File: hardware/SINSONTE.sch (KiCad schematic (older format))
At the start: 31 parts, among them J1 BAT, J10 Conn_01x01_Male, J11 Conn_01x01_Male, J12 Conn_01x04_Male, J13 Conn_01x01_Male, J14 Conn_01x02_Male, J2 CLOCK, J3 LIGHT_SENSOR, J4 Conn_01x17_Male, J5 Conn_01x01_Male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

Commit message: add note to change R1 for CP
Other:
- note added: "Increase to 470K\nfor CircuitPython"
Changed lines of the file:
@@
 Wire Wire Line
 	6950 5000 9000 5000
+Text Notes 3150 3350 0    50   ~ 0
+Increase to 470K\nfor CircuitPython
 $EndSCHEMATC

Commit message: changed ext batt for screw terminal type
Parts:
- J1: footprint Connector_PinHeader_2.54mm:PinHeader_1x02_P2.54mm_Vertical -> TerminalBlock_4Ucon:TerminalBlock_4Ucon_1x02_P3.50mm_Horizontal
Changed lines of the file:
@@
 F 0 "J1" H 2800 2800 50  0000 C CNN
 F 1 "BAT" H 2800 2700 50  0000 C CNN
-F 2 "Connector_PinHeader_2.54mm:PinHeader_1x02_P2.54mm_Vertical" H 2950 2750 50  0001 C CNN
+F 2 "TerminalBlock_4Ucon:TerminalBlock_4Ucon_1x02_P3.50mm_Horizontal" H 2950 2750 50  0001 C CNN
 F 3 "~" H 2950 2750 50  0001 C CNN
 	1    2950 2750

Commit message: rpi first half conn aded 1 pos on ground
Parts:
- removed J4: Conn_01x17_Male, Connector_PinHeader_2.54mm:PinHeader_1x17_P2.54mm_Vertical, symbol Connector:Conn_01x17_Male
- added J15: Conn_01x01_Male, Connector_PinHeader_2.54mm:PinHeader_1x01_P2.54mm_Vertical, symbol Connector:Conn_01x01_Male
- added J4: Conn_01x18_Male, Connector_PinHeader_2.54mm:PinHeader_1x18_P2.54mm_Vertical, symbol Connector:Conn_01x18_Male
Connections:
- wire segments 144 -> 146
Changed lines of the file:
@@
 	9000 3350 9000 5000
-$Comp
-L Connector:Conn_01x17_Male J4
-U 1 1 604C5DB6
-P 4550 3350
-F 0 "J4" H 4658 4331 50  0000 C CNN
-F 1 "Conn_01x17_Male" H 4658 4240 50  0000 C CNN
-F 2 "Connector_PinHeader_2.54mm:PinHeader_1x17_P2.54mm_Vertical" H 4550 3350 50  0001 C CNN
-F 3 "~" H 4550 3350 50  0001 C CNN
-	1    4550 3350
-	1    0    0    -1
-$EndComp
-Wire Wire Line
-	4750 2550 4900 2550
-Wire Wire Line
-	4750 2650 4900 2650
-Wire Wire Line
-	4750 2750 4800 2750
-Wire Wire Line
-	4750 2850 4900 2850
-Wire Wire Line
-	4750 2950 4900 2950
-Wire Wire Line
-	4750 3050 4900 3050
-Wire Wire Line
-	4750 3150 4900 3150
-Wire Wire Line
-	4750 3250 4800 3250
-Wire Wire Line
-	4750 3350 4900 3350
-Wire Wire Line
-	4750 3450 4900 3450
-Wire Wire Line
-	4750 3550 4900 3550
-Wire Wire Line
-	4750 3650 4900 3650
-Wire Wire Line
-	4750 3750 4800 3750
-Wire Wire Line
-	4750 3850 4900 3850
-Wire Wire Line
-	4750 3950 4900 3950
-Wire Wire Line
-	4750 4050 4900 4050
-Wire Wire Line
-	4750 4150 4900 4150
 $Comp
 L Connector:Conn_01x01_Male J5
@@
 Connection ~ 4800 4250
 Wire Wire Line
-	4800 4250 4600 4250
+	4800 4250 4700 4250
 Wire Wire Line
 	6400 3250 6450 3250
@@
 Text Notes 3150 3350 0    50   ~ 0
 Increase to 470K\nfor CircuitPython
+$Comp
+L Connector:Conn_01x18_Male J4
+U 1 1 618ACA73
+P 4500 3350
+F 0 "J4" H 4608 4331 50  0000 C CNN
+F 1 "Conn_01x18_Male" H 4608 4240 50  0000 C CNN
+F 2 "Connector_PinHeader_2.54mm:PinHeader_1x18_P2.54mm_Vertical" H 4500 3350 50  0001 C CNN
+F 3 "~" H 4500 3350 50  0001 C CNN
+	1    4500 3350
+	1    0    0    -1
+$EndComp
+Connection ~ 4700 4250
+Wire Wire Line
+	4700 4250 4600 4250
+Wire Wire Line
+	4700 2550 4900 2550
+Wire Wire Line
+	4700 2650 4900 2650
+Wire Wire Line
+	4700 2750 4800 2750
+Wire Wire Line
+	4700 2850 4900 2850
+Wire Wire Line
+	4700 2950 4900 2950
+Wire Wire Line
+	4700 3050 4900 3050
+Wire Wire Line
+	4700 3150 4900 3150
+Wire Wire Line
+	4700 3250 4800 3250
+Wire Wire Line
+	4700 3350 4900 3350
+Wire Wire Line
+	4700 3450 4900 3450
+Wire Wire Line
+	4700 3550 4900 3550
+Wire Wire Line
+	4700 3650 4900 3650
+Wire Wire Line
+	4700 3750 4800 3750
+Wire Wire Line
+	4700 3850 4900 3850
+Wire Wire Line
+	4700 3950 4900 3950
+Wire Wire Line
+	4700 4050 4900 4050
+Wire Wire Line
+	4700 4150 4900 4150
+$Comp
+L Connector:Conn_01x01_Male J15
+U 1 1 6193CA8B
+P 4500 4450
+F 0 "J15" H 4608 4631 50  0000 C CNN
+F 1 "Conn_01x01_Male" H 4608 4540 50  0000 C CNN
+F 2 "Connector_PinHeader_2.54mm:PinHeader_1x01_P2.54mm_Vertical" H 4500 4450 50  0001 C CNN
+F 3 "~" H 4500 4450 50  0001 C CNN
+	1    4500 4450
+	1    0    0    -1
+$EndComp
+Wire Wire Line
+	4700 4450 4800 4450
+Connection ~ 4800 4450
 $EndSCHEMATC

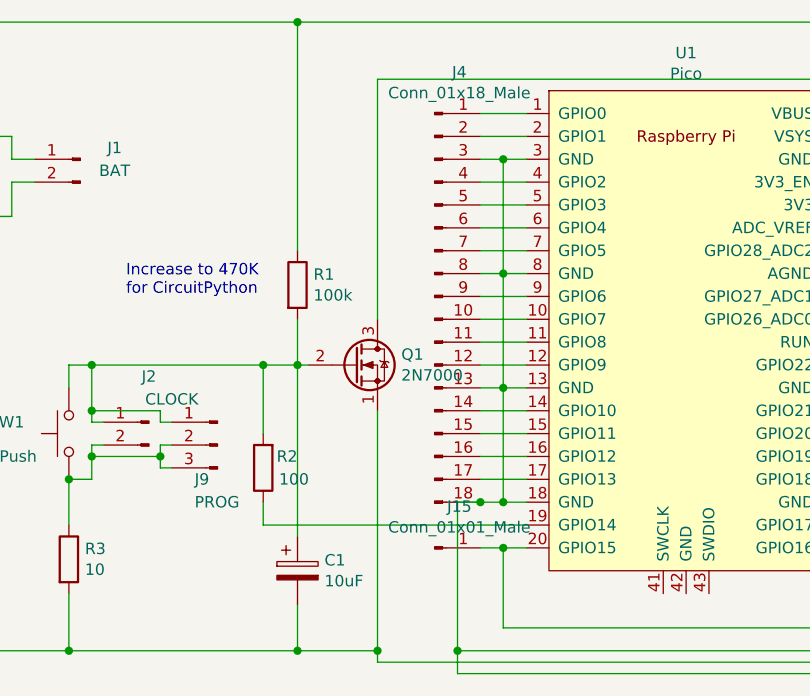
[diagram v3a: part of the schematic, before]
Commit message: rpi first half conn aded all pins connector
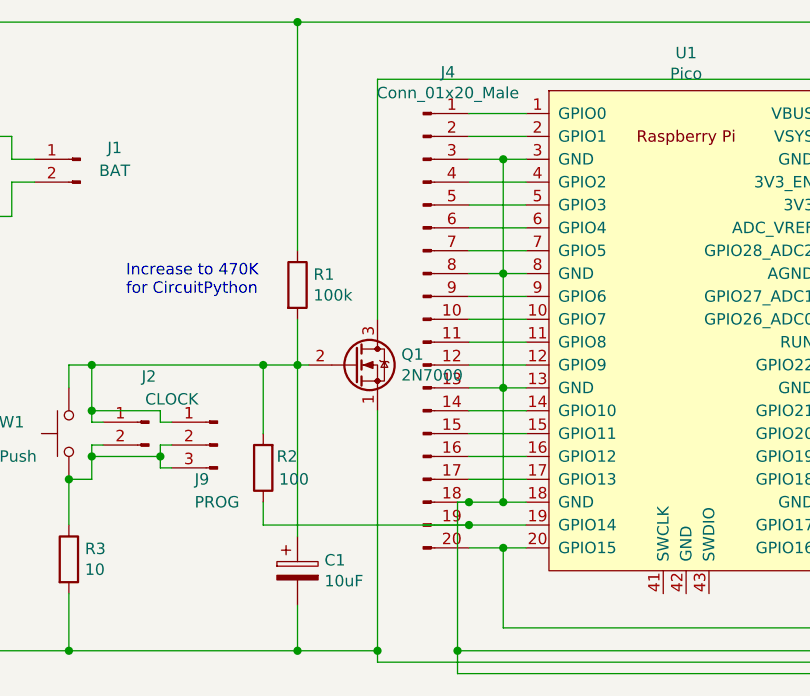
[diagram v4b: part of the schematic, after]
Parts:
- removed J15: Conn_01x01_Male, Connector_PinHeader_2.54mm:PinHeader_1x01_P2.54mm_Vertical, symbol Connector:Conn_01x01_Male
- removed J4: Conn_01x18_Male, Connector_PinHeader_2.54mm:PinHeader_1x18_P2.54mm_Vertical, symbol Connector:Conn_01x18_Male
- added J4: Conn_01x20_Male, Connector_PinHeader_2.54mm:PinHeader_1x20_P2.54mm_Vertical, symbol Connector:Conn_01x20_Male
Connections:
- net at U1.1 (GPIO0): now also J4.1 (Pin_1)
- net at U1.10 (GPIO7): now also J4.10 (Pin_10)
- net at U1.11 (GPIO8): now also J4.11 (Pin_11)
- net at U1.12 (GPIO9): now also J4.12 (Pin_12)
- net at BT1.2 (-), C1.2, C2.2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: now also J4.13 (Pin_13), J4.18 (Pin_18), J4.3 (Pin_3), J4.8 (Pin_8)
- net at U1.14 (GPIO10): now also J4.14 (Pin_14)
- net at U1.15 (GPIO11): now also J4.15 (Pin_15)
- net at U1.16 (GPIO12): now also J4.16 (Pin_16)
- net at U1.17 (GPIO13): now also J4.17 (Pin_17)
- net at R2.1, U1.19 (GPIO14): now also J4.19 (Pin_19)
- net at U1.2 (GPIO1): now also J4.2 (Pin_2)
- net at R8.1, U1.20 (GPIO15): now also J4.20 (Pin_20)
- net at U1.4 (GPIO2): now also J4.4 (Pin_4)
- net at U1.5 (GPIO3): now also J4.5 (Pin_5)
- net at U1.6 (GPIO4): now also J4.6 (Pin_6)
- net at U1.7 (GPIO5): now also J4.7 (Pin_7)
- net at U1.9 (GPIO6): now also J4.9 (Pin_9)
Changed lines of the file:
@@
 Connection ~ 3900 3650
 Wire Wire Line
-	3750 4350 4900 4350
+	3750 4350 4650 4350
 Wire Wire Line
 	3900 4700 3900 4900
@@
 Connection ~ 4800 4250
 Wire Wire Line
-	4800 4250 4700 4250
-Wire Wire Line
 	6400 3250 6450 3250
 Connection ~ 6400 3250
@@
 Text Notes 3150 3350 0    50   ~ 0
 Increase to 470K\nfor CircuitPython
-$Comp
-L Connector:Conn_01x18_Male J4
-U 1 1 618ACA73
-P 4500 3350
-F 0 "J4" H 4608 4331 50  0000 C CNN
-F 1 "Conn_01x18_Male" H 4608 4240 50  0000 C CNN
-F 2 "Connector_PinHeader_2.54mm:PinHeader_1x18_P2.54mm_Vertical" H 4500 3350 50  0001 C CNN
-F 3 "~" H 4500 3350 50  0001 C CNN
-	1    4500 3350
+Connection ~ 4800 4450
+Wire Wire Line
+	4600 4250 4650 4250
+$Comp
+L Connector:Conn_01x20_Male J4
+U 1 1 618AE8C2
+P 4450 3450
+F 0 "J4" H 4558 4531 50  0000 C CNN
+F 1 "Conn_01x20_Male" H 4558 4440 50  0000 C CNN
+F 2 "Connector_PinHeader_2.54mm:PinHeader_1x20_P2.54mm_Vertical" H 4450 3450 50  0001 C CNN
+F 3 "~" H 4450 3450 50  0001 C CNN
+	1    4450 3450
 	1    0    0    -1
 $EndComp
-Connection ~ 4700 4250
-Wire Wire Line
-	4700 4250 4600 4250
-Wire Wire Line
-	4700 2550 4900 2550
-Wire Wire Line
-	4700 2650 4900 2650
-Wire Wire Line
-	4700 2750 4800 2750
-Wire Wire Line
-	4700 2850 4900 2850
-Wire Wire Line
-	4700 2950 4900 2950
-Wire Wire Line
-	4700 3050 4900 3050
-Wire Wire Line
-	4700 3150 4900 3150
-Wire Wire Line
-	4700 3250 4800 3250
-Wire Wire Line
-	4700 3350 4900 3350
-Wire Wire Line
-	4700 3450 4900 3450
-Wire Wire Line
-	4700 3550 4900 3550
-Wire Wire Line
-	4700 3650 4900 3650
-Wire Wire Line
-	4700 3750 4800 3750
-Wire Wire Line
-	4700 3850 4900 3850
-Wire Wire Line
-	4700 3950 4900 3950
-Wire Wire Line
-	4700 4050 4900 4050
-Wire Wire Line
-	4700 4150 4900 4150
-$Comp
-L Connector:Conn_01x01_Male J15
-U 1 1 6193CA8B
-P 4500 4450
-F 0 "J15" H 4608 4631 50  0000 C CNN
-F 1 "Conn_01x01_Male" H 4608 4540 50  0000 C CNN
-F 2 "Connector_PinHeader_2.54mm:PinHeader_1x01_P2.54mm_Vertical" H 4500 4450 50  0001 C CNN
-F 3 "~" H 4500 4450 50  0001 C CNN
-	1    4500 4450
-	1    0    0    -1
-$EndComp
-Wire Wire Line
-	4700 4450 4800 4450
-Connection ~ 4800 4450
+Connection ~ 4650 4250
+Wire Wire Line
+	4650 4250 4800 4250
+Connection ~ 4650 4350
+Wire Wire Line
+	4650 4350 4900 4350
+Wire Wire Line
+	4650 2550 4900 2550
+Wire Wire Line
+	4650 2650 4900 2650
+Wire Wire Line
+	4650 2750 4800 2750
+Wire Wire Line
+	4650 2850 4900 2850
+Wire Wire Line
+	4650 2950 4900 2950
+Wire Wire Line
+	4650 3050 4900 3050
+Wire Wire Line
+	4650 3150 4900 3150
+Wire Wire Line
+	4650 3250 4800 3250
+Wire Wire Line
+	4650 3350 4900 3350
+Wire Wire Line
+	4650 3450 4900 3450
+Wire Wire Line
+	4650 3550 4900 3550
+Wire Wire Line
+	4650 3650 4900 3650
+Wire Wire Line
+	4650 3750 4800 3750
+Wire Wire Line
+	4650 3850 4900 3850
+Wire Wire Line
+	4650 3950 4900 3950
+Wire Wire Line
+	4650 4050 4900 4050
+Wire Wire Line
+	4650 4150 4900 4150
+Wire Wire Line
+	4650 4450 4800 4450
 $EndSCHEMATC

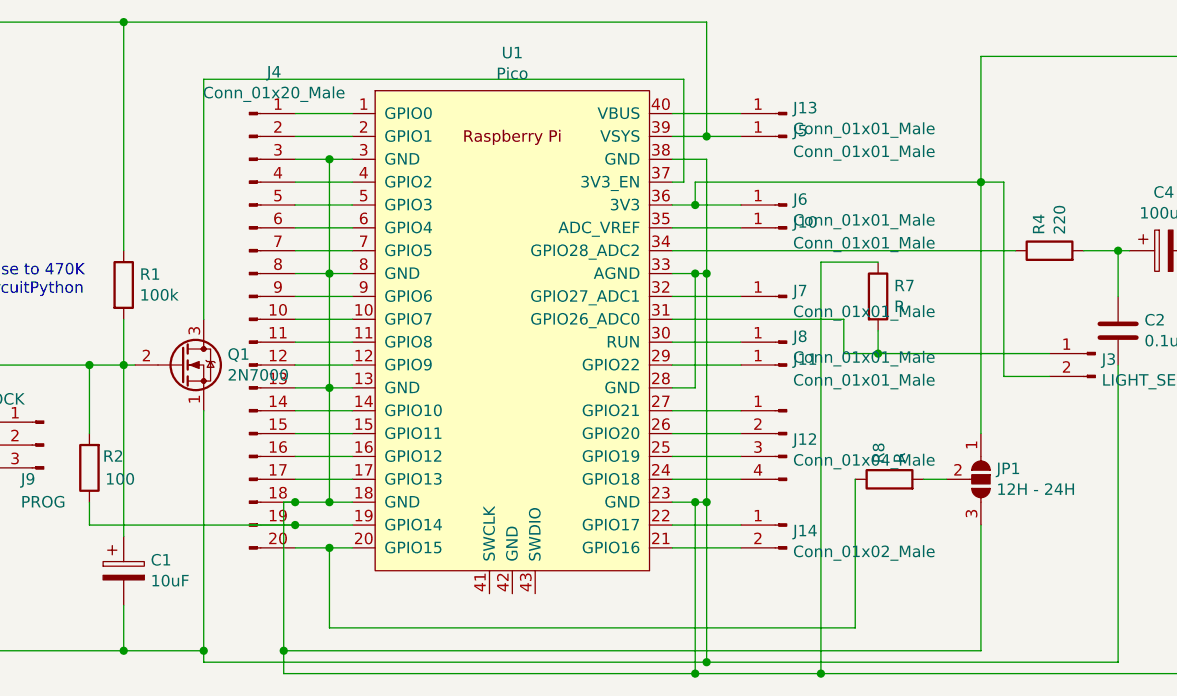
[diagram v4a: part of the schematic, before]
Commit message: rpi second half conn aded all pins connector
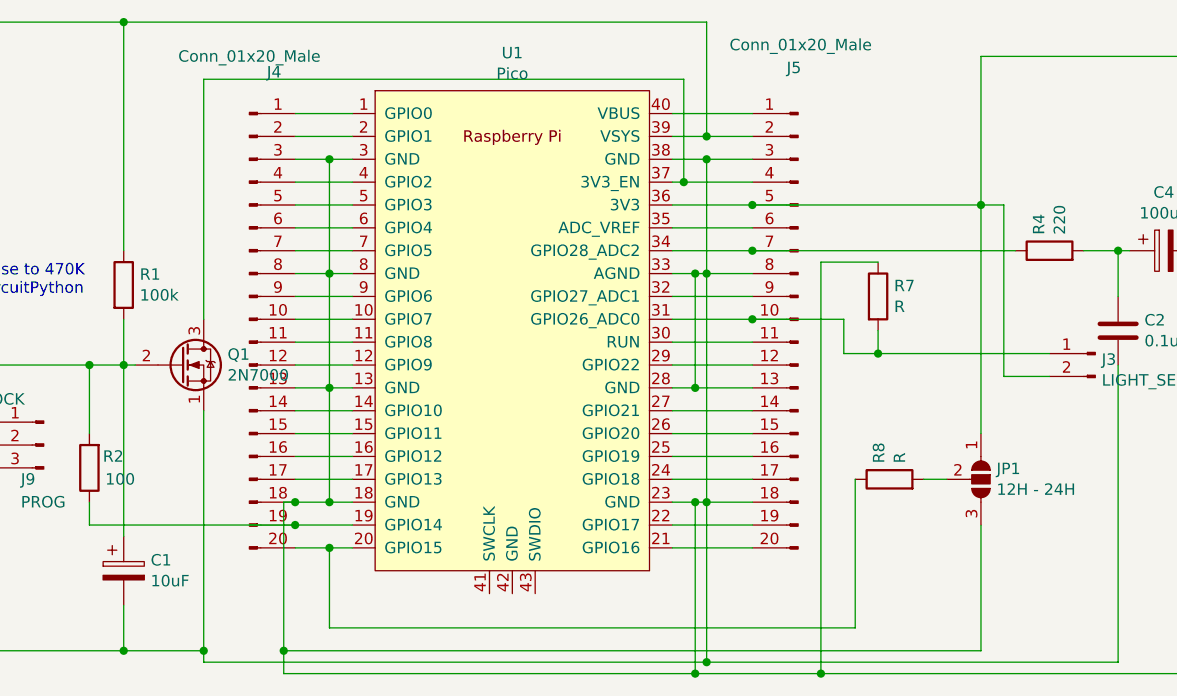
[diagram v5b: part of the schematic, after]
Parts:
- removed J10, J11, J13, J5, J6, J7, J8: Conn_01x01_Male, Connector_PinHeader_2.54mm:PinHeader_1x01_P2.54mm_Vertical, symbol Connector:Conn_01x01_Male
- removed J12: Conn_01x04_Male, Connector_PinHeader_2.54mm:PinHeader_1x04_P2.54mm_Vertical, symbol Connector:Conn_01x04_Male
- removed J14: Conn_01x02_Male, Connector_PinHeader_2.54mm:PinHeader_1x02_P2.54mm_Vertical, symbol Connector:Conn_01x02_Male
- added J5: Conn_01x20_Male, Connector_PinHeader_2.54mm:PinHeader_1x20_P2.54mm_Vertical, symbol Connector:Conn_01x20_Male
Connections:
- net at BT1.2 (-), C1.2, C2.2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: now also J5.13 (Pin_13), J5.18 (Pin_18), J5.3 (Pin_3), J5.8 (Pin_8)
- net at U1.21 (GPIO16): now also J5.20 (Pin_20)
- net at U1.22 (GPIO17): now also J5.19 (Pin_19)
- net at U1.24 (GPIO18): now also J5.17 (Pin_17)
- net at U1.25 (GPIO19): now also J5.16 (Pin_16)
- net at U1.26 (GPIO20): now also J5.15 (Pin_15)
- net at U1.27 (GPIO21): now also J5.14 (Pin_14)
- net at U1.29 (GPIO22): now also J5.12 (Pin_12)
- net at U1.30 (RUN): now also J5.11 (Pin_11)
- net at J3.1 (Pin_1), R7.2, U1.31 (GPIO26_ADC0): now also J5.10 (Pin_10)
- net at U1.32 (GPIO27_ADC1): now also J5.9 (Pin_9)
- net at R4.1, U1.34 (GPIO28_ADC2): now also J5.7 (Pin_7)
- net at U1.35 (ADC_VREF): now also J5.6 (Pin_6)
- net at J3.2 (Pin_2), JP1.1 (A), LS1.1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: now also J5.5 (Pin_5)
- net at Q1.3 (D), U1.37 (3V3_EN): now also J5.4 (Pin_4)
- net at BT1.1 (+), J1.1 (Pin_1), R1.1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: now also J5.2 (Pin_2)
- net at U1.40 (VBUS): now also J5.1 (Pin_1)
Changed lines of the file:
@@
 Wire Wire Line
 	8100 3150 8250 3150
-Wire Wire Line
-	7800 3150 6300 3150
 $Comp
 L Device:CP C4
@@
 $EndComp
 Wire Wire Line
-	6300 3450 7050 3450
-Wire Wire Line
 	7050 3450 7050 3600
 Wire Wire Line
@@
 Wire Wire Line
 	9000 3350 9000 5000
-$Comp
-L Connector:Conn_01x01_Male J5
-U 1 1 604D8356
-P 6800 2650
-F 0 "J5" H 6772 2674 50  0000 R CNN
-F 1 "Conn_01x01_Male" H 6772 2583 50  0000 R CNN
-F 2 "Connector_PinHeader_2.54mm:PinHeader_1x01_P2.54mm_Vertical" H 6800 2650 50  0001 C CNN
-F 3 "~" H 6800 2650 50  0001 C CNN
-	1    6800 2650
-	-1   0    0    -1
-$EndComp
 Wire Wire Line
 	4600 4900 7650 4900
 Wire Wire Line
 	4800 4800 7100 4800
-Wire Wire Line
-	6600 2650 6450 2650
 Connection ~ 6450 2650
 Wire Wire Line
-	7650 2850 7650 3950
-Wire Wire Line
-	6400 2950 6300 2950
-$Comp
-L Connector:Conn_01x01_Male J6
-U 1 1 605AAAE1
-P 6800 2950
-F 0 "J6" H 6772 2974 50  0000 R CNN
-F 1 "Conn_01x01_Male" H 6772 2883 50  0000 R CNN
-F 2 "Connector_PinHeader_2.54mm:PinHeader_1x01_P2.54mm_Vertical" H 6800 2950 50  0001 C CNN
-F 3 "~" H 6800 2950 50  0001 C CNN
-	1    6800 2950
-	-1   0    0    -1
-$EndComp
-Wire Wire Line
-	6400 2950 6600 2950
-Connection ~ 6400 2950
-$Comp
-L Connector:Conn_01x01_Male J7
-U 1 1 605B1189
-P 6800 3350
-F 0 "J7" H 6772 3374 50  0000 R CNN
-F 1 "Conn_01x01_Male" H 6772 3283 50  0000 R CNN
-F 2 "Connector_PinHeader_2.54mm:PinHeader_1x01_P2.54mm_Vertical" H 6800 3350 50  0001 C CNN
-F 3 "~" H 6800 3350 50  0001 C CNN
-	1    6800 3350
-	-1   0    0    -1
-$EndComp
-Wire Wire Line
-	6300 3350 6600 3350
-Wire Wire Line
 	6300 3250 6400 3250
 Wire Wire Line
@@
 Wire Wire Line
 	6400 3750 6300 3750
-$Comp
-L Connector:Conn_01x01_Male J8
-U 1 1 605C10F3
-P 6800 3550
-F 0 "J8" H 6772 3574 50  0000 R CNN
-F 1 "Conn_01x01_Male" H 6772 3483 50  0000 R CNN
-F 2 "Connector_PinHeader_2.54mm:PinHeader_1x01_P2.54mm_Vertical" H 6800 3550 50  0001 C CNN
-F 3 "~" H 6800 3550 50  0001 C CNN
-	1    6800 3550
-	-1   0    0    -1
-$EndComp
-Wire Wire Line
-	6300 3550 6600 3550
 Wire Wire Line
 	9000 2400 9000 2300
@@
 	9000 2300 7650 2300
 Wire Wire Line
-	7650 2300 7650 2850
-Connection ~ 7650 2850
+	7650 2300 7650 2950
+Connection ~ 7650 2950
 Wire Wire Line
 	4600 4250 4600 4900
@@
 Connection ~ 4250 4900
 Wire Wire Line
-	6400 2850 6400 2950
-$Comp
-L Connector:Conn_01x01_Male J10
-U 1 1 6082CC33
-P 6800 3050
-F 0 "J10" H 6772 3074 50  0000 R CNN
-F 1 "Conn_01x01_Male" H 6772 2983 50  0000 R CNN
-F 2 "Connector_PinHeader_2.54mm:PinHeader_1x01_P2.54mm_Vertical" H 6800 3050 50  0001 C CNN
-F 3 "~" H 6800 3050 50  0001 C CNN
-	1    6800 3050
-	-1   0    0    -1
-$EndComp
-Wire Wire Line
-	6300 3050 6600 3050
-$Comp
-L Connector:Conn_01x01_Male J11
-U 1 1 60836840
-P 6800 3650
-F 0 "J11" H 6772 3674 50  0000 R CNN
-F 1 "Conn_01x01_Male" H 6772 3583 50  0000 R CNN
-F 2 "Connector_PinHeader_2.54mm:PinHeader_1x01_P2.54mm_Vertical" H 6800 3650 50  0001 C CNN
-F 3 "~" H 6800 3650 50  0001 C CNN
-	1    6800 3650
-	-1   0    0    -1
-$EndComp
-Wire Wire Line
-	6300 3650 6600 3650
-Wire Wire Line
 	6450 2750 6450 3250
-$Comp
-L Connector:Conn_01x04_Male J12
-U 1 1 6084391D
-P 6800 3950
-F 0 "J12" H 6772 3924 50  0000 R CNN
-F 1 "Conn_01x04_Male" H 6772 3833 50  0000 R CNN
-F 2 "Connector_PinHeader_2.54mm:PinHeader_1x04_P2.54mm_Vertical" H 6800 3950 50  0001 C CNN
-F 3 "~" H 6800 3950 50  0001 C CNN
-	1    6800 3950
-	-1   0    0    -1
-$EndComp
-Wire Wire Line
-	6300 3850 6600 3850
-Wire Wire Line
-	6300 3950 6600 3950
-Wire Wire Line
-	6300 4050 6600 4050
-Wire Wire Line
-	6300 4150 6600 4150
-$Comp
-L Connector:Conn_01x01_Male J13
-U 1 1 60872957
-P 6800 2550
-F 0 "J13" H 6772 2574 50  0000 R CNN
-F 1 "Conn_01x01_Male" H 6772 2483 50  0000 R CNN
-F 2 "Connector_PinHeader_2.54mm:PinHeader_1x01_P2.54mm_Vertical" H 6800 2550 50  0001 C CNN
-F 3 "~" H 6800 2550 50  0001 C CNN
-	1    6800 2550
-	-1   0    0    -1
-$EndComp
-Wire Wire Line
-	6300 2550 6600 2550
 $Comp
 L Connector:Conn_01x03_Male J9
@@
 Wire Wire Line
 	3000 4050 3000 4150
-$Comp
-L Connector:Conn_01x02_Male J14
-U 1 1 608B2996
-P 6800 4350
-F 0 "J14" H 6772 4324 50  0000 R CNN
-F 1 "Conn_01x02_Male" H 6772 4233 50  0000 R CNN
-F 2 "Connector_PinHeader_2.54mm:PinHeader_1x02_P2.54mm_Vertical" H 6800 4350 50  0001 C CNN
-F 3 "~" H 6800 4350 50  0001 C CNN
-	1    6800 4350
-	-1   0    0    -1
-$EndComp
-Wire Wire Line
-	6300 4350 6600 4350
-Wire Wire Line
-	6300 4450 6600 4450
 Wire Wire Line
 	4800 2750 4800 3250
@@
 	6400 5000 6950 5000
 Wire Wire Line
-	7750 3700 7750 2850
-Wire Wire Line
-	7750 2850 7650 2850
+	7750 3700 7750 2950
+Wire Wire Line
+	7750 2950 7650 2950
 Wire Wire Line
 	7750 3700 7950 3700
-Wire Wire Line
-	6400 2850 7650 2850
 Wire Wire Line
 	7200 3200 6950 3200
@@
 P 4450 3450
 F 0 "J4" H 4558 4531 50  0000 C CNN
-F 1 "Conn_01x20_Male" H 4558 4440 50  0000 C CNN
+F 1 "Conn_01x20_Male" H 4450 4600 50  0000 C CNN
 F 2 "Connector_PinHeader_2.54mm:PinHeader_1x20_P2.54mm_Vertical" H 4450 3450 50  0001 C CNN
 F 3 "~" H 4450 3450 50  0001 C CNN
@@
 Wire Wire Line
 	4650 4450 4800 4450
+Wire Wire Line
+	6300 2550 6650 2550
+Wire Wire Line
+	6450 2650 6650 2650
+Wire Wire Line
+	6450 2750 6650 2750
+Connection ~ 6450 2750
+Wire Wire Line
+	6300 3050 6650 3050
+Wire Wire Line
+	6450 3250 6650 3250
+Wire Wire Line
+	6300 3350 6650 3350
+Wire Wire Line
+	6300 3550 6650 3550
+Wire Wire Line
+	6300 3650 6650 3650
+Wire Wire Line
+	6650 3750 6400 3750
+Connection ~ 6400 3750
+Wire Wire Line
+	6300 3850 6650 3850
+Wire Wire Line
+	6300 3950 6650 3950
+Wire Wire Line
+	6300 4050 6650 4050
+Wire Wire Line
+	6300 4150 6650 4150
+Wire Wire Line
+	6650 4250 6450 4250
+Wire Wire Line
+	6300 4350 6650 4350
+Wire Wire Line
+	6300 4450 6650 4450
+Wire Wire Line
+	6650 3150 6300 3150
+Wire Wire Line
+	7800 3150 6650 3150
+Connection ~ 6650 3150
+Wire Wire Line
+	6650 3450 7050 3450
+Wire Wire Line
+	6300 3450 6650 3450
+Connection ~ 6650 3450
+$Comp
+L Connector:Conn_01x20_Male J5
+U 1 1 618B0A3E
+P 6850 3450
+F 0 "J5" H 6900 4550 50  0000 R CNN
+F 1 "Conn_01x20_Male" H 7150 4650 50  0000 R CNN
+F 2 "Connector_PinHeader_2.54mm:PinHeader_1x20_P2.54mm_Vertical" H 6850 3450 50  0001 C CNN
+F 3 "~" H 6850 3450 50  0001 C CNN
+	1    6850 3450
+	-1   0    0    -1
+$EndComp
+Wire Wire Line
+	7650 2950 7650 3950
+Connection ~ 6650 2950
+Wire Wire Line
+	6650 2950 7650 2950
+Wire Wire Line
+	6300 2950 6650 2950
+Wire Wire Line
+	6350 2850 6650 2850
+Connection ~ 6350 2850
 $EndSCHEMATC
